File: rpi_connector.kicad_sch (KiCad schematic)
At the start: 2 parts, among them J3 DF40HC_3.0_-100DS-0.4V_58, J4 DF40HC_3.0_-100DS-0.4V_58

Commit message: pcb changes
GPIO-cons routed (what a mess)
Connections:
- net GPIO 26 renamed GPIO26

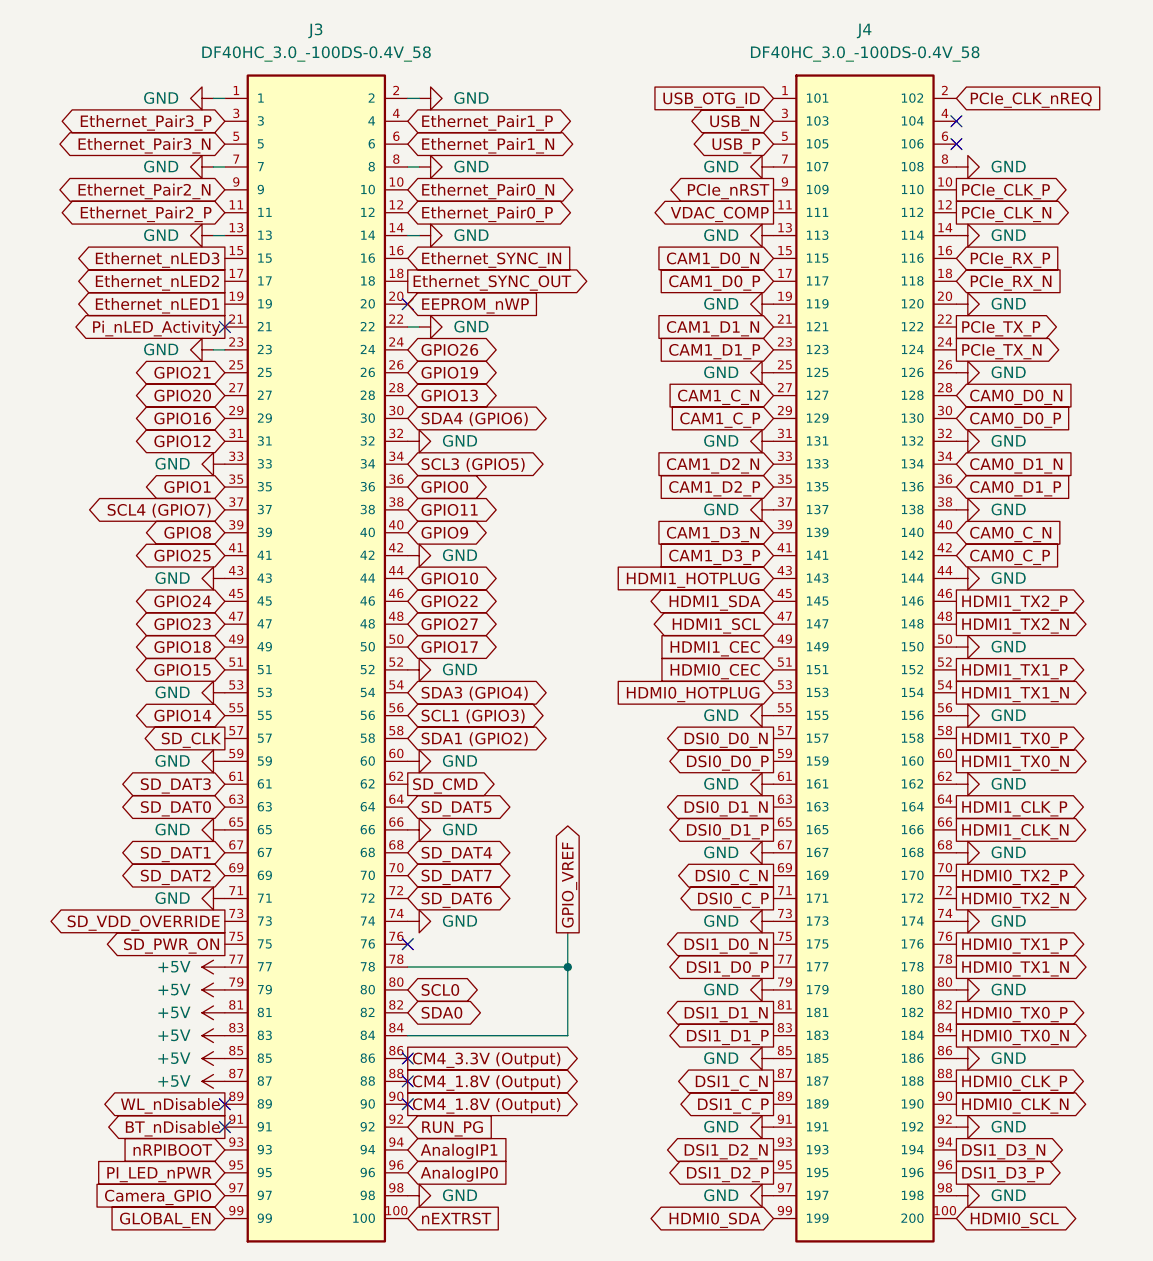
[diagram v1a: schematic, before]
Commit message: CM4>RP3/4
changed SBC to RP3/4
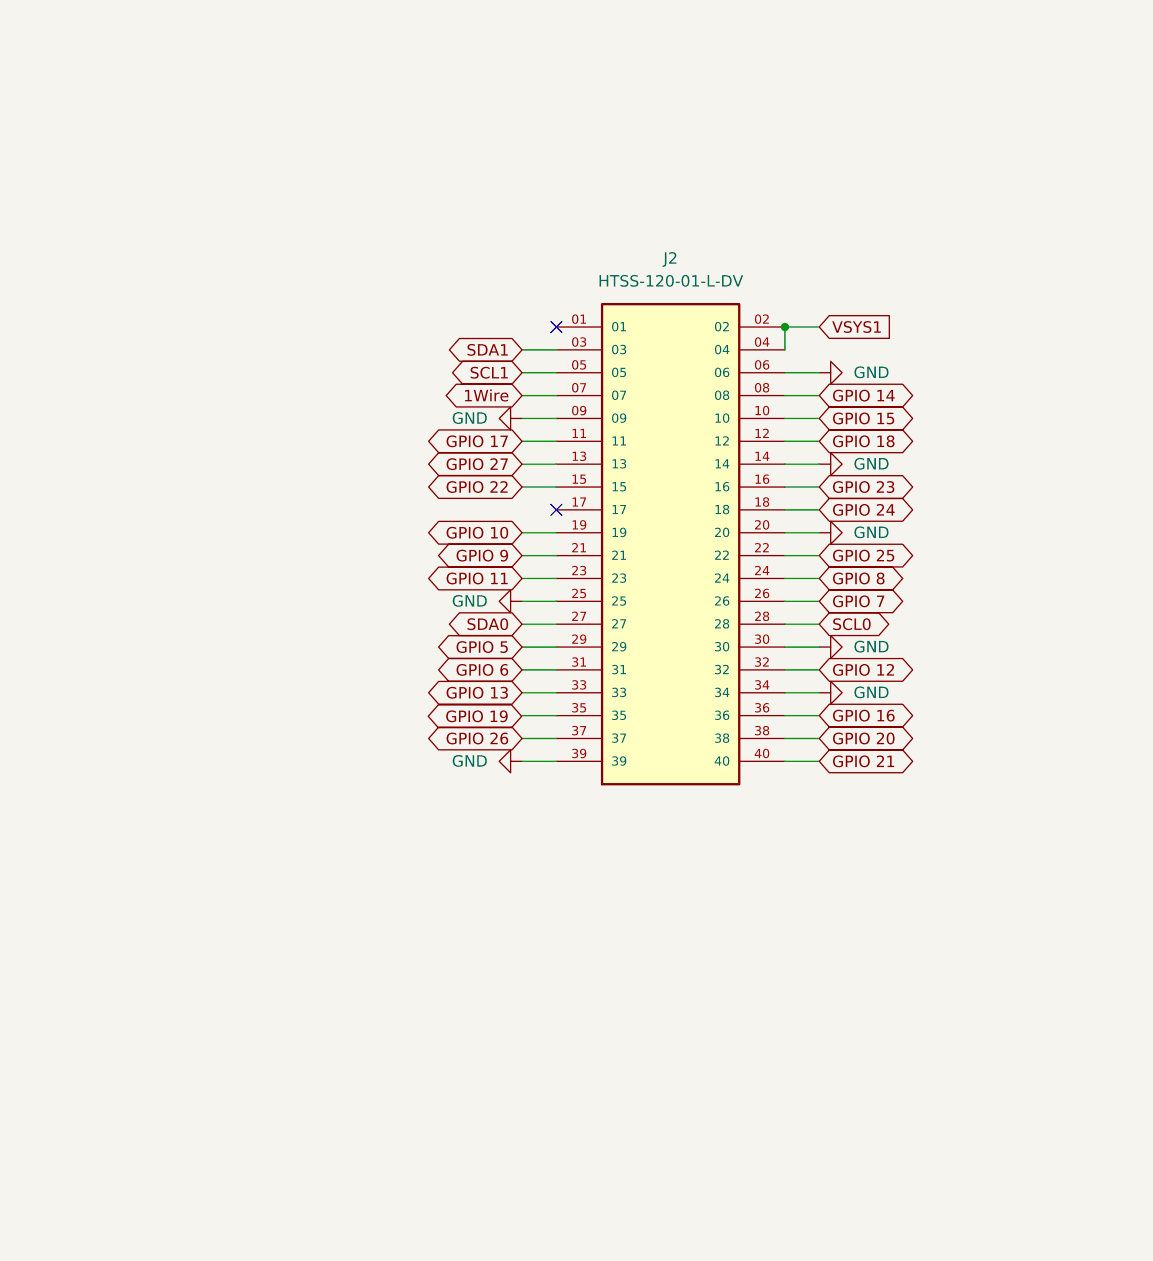
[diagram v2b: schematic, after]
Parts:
- removed J3, J4: DF40HC_3.0_-100DS-0.4V_58, connectors_Hirose:HRS_DF40HC_3.0_-100DS-0.4V_58, symbol connectors_Hirose:DF40HC_3.0_-100DS-0.4V_58
- added J2: HTSS-120-01-L-DV, HTSS-120-01-L-DV:SAMTEC_HTSS-120-01-L-DV, symbol HTSS-120-01-L-DV:HTSS-120-01-L-DV
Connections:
- net GND: now also J2.06, J2.09, J2.14, J2.20, J2.25, J2.30, J2.34, J2.39
- net SCL0: now also J2.28
- net SDA0: now also J2.27
- new net 1Wire: J2.07
- new net GPIO 10: J2.19
- new net GPIO 11: J2.23
- new net GPIO 12: J2.32
- new net GPIO 13: J2.33
- new net GPIO 14: J2.08
- new net GPIO 15: J2.10
- new net GPIO 16: J2.36
- new net GPIO 17: J2.11
- new net GPIO 18: J2.12
- new net GPIO 20: J2.38
- new net GPIO 21: J2.40
- new net GPIO 22: J2.15
- new net GPIO 23: J2.16
- new net GPIO 24: J2.18
- new net GPIO 25: J2.22
- new net GPIO 26: J2.37
- new net GPIO 27: J2.13
- new net GPIO 5: J2.29
- new net GPIO 6: J2.31
- new net GPIO 7: J2.26
- new net GPIO 8: J2.24
- new net GPIO 9: J2.21
- new net SCL1: J2.05
- new net SDA1: J2.03
- new net VSYS1: J2.02, J2.04
- no-connect marks 10 -> 2
